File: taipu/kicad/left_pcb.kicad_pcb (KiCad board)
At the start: 2 copper layers, 145 x 92.4 mm, 52 parts

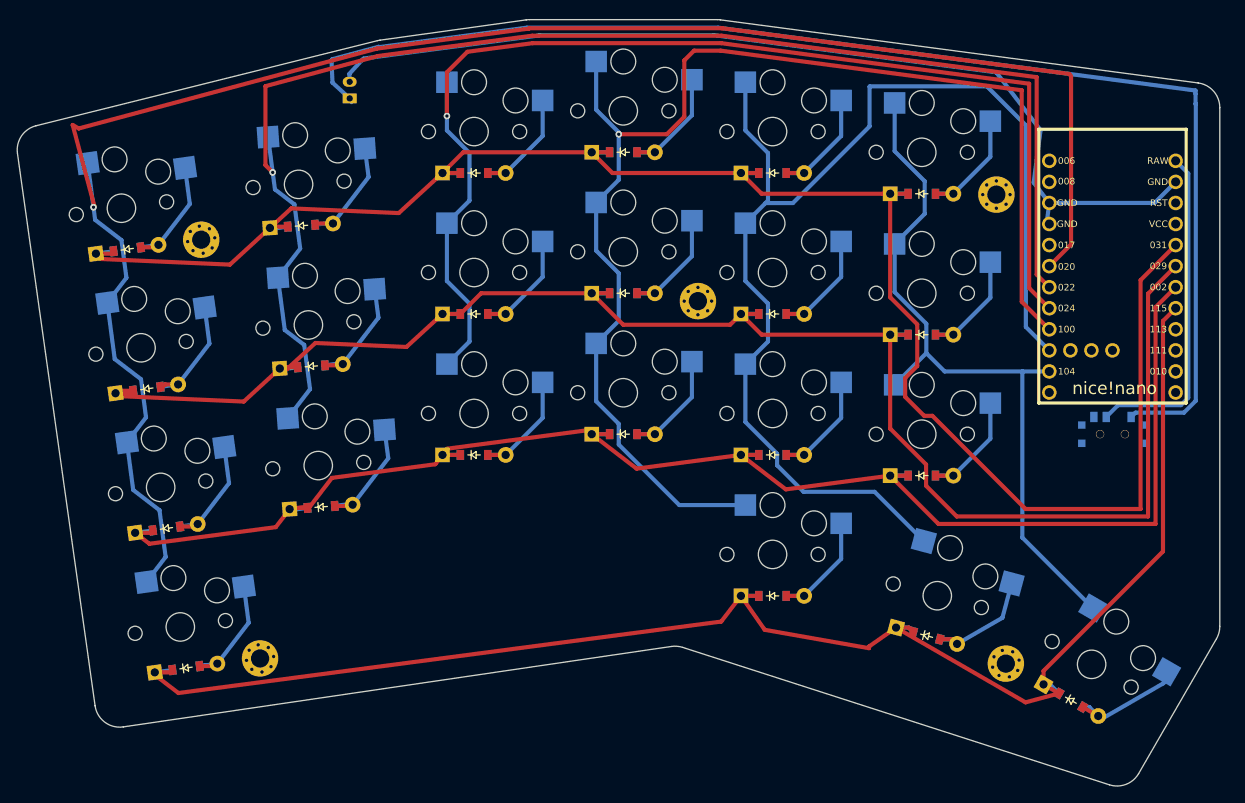
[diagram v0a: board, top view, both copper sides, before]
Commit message: better batery placement
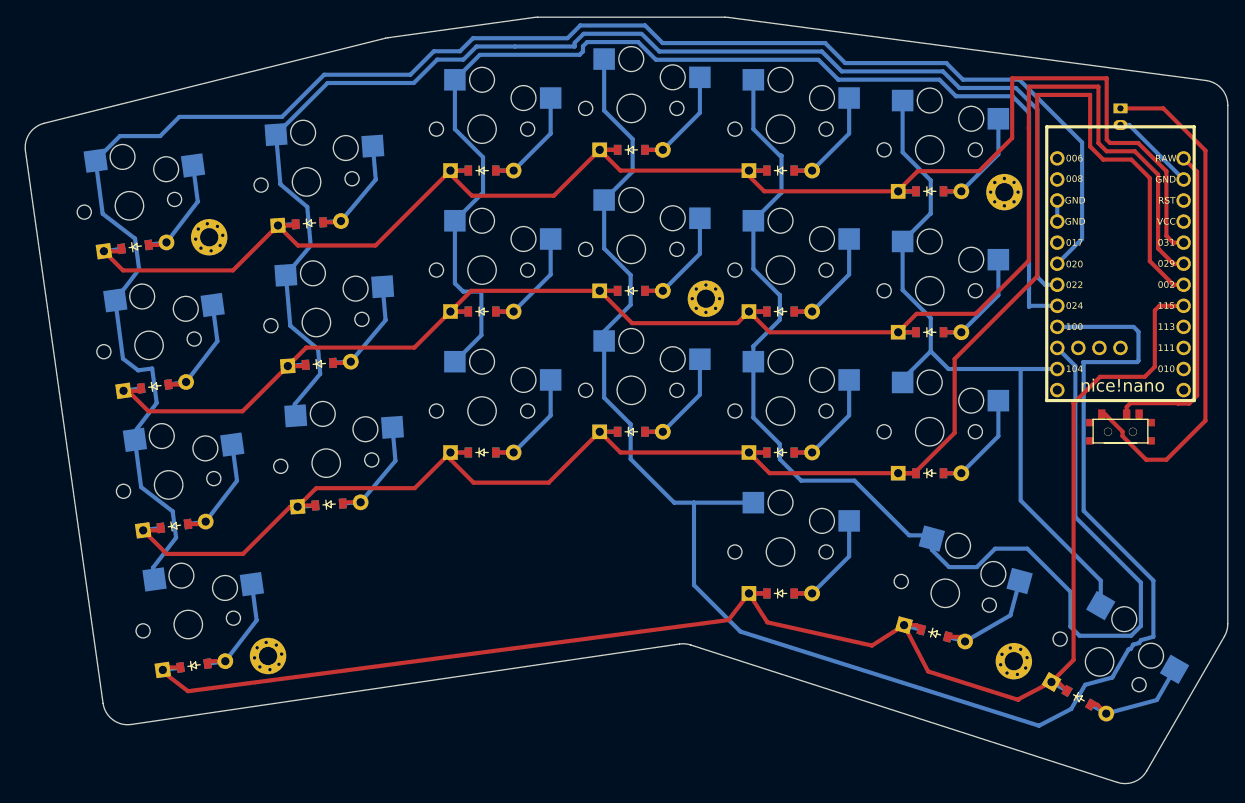
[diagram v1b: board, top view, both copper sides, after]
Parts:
- moved JST1 93.0 mm to (199.5, 87.0), turned to -90 degrees
- moved S5 1.01 mm to (103.7, 128.8)
- moved S6 1.01 mm to (102.5, 111.9)
- moved D16 1.01 mm to (158.5, 110.5)
- moved _1 1.01 mm to (89.6, 101.6)
- moved S19 1.01 mm to (176.5, 108.0)
- moved S17 1.01 mm to (158.5, 88.5)
- moved D9 1.01 mm to (122.5, 110.5)
- moved D2 1.01 mm to (85.4, 136.4)
- moved D14 1.01 mm to (158.5, 144.5)
- moved S3 1.01 mm to (82.3, 114.6)
- moved D19 1.01 mm to (176.5, 113.0)
- moved S20 1.01 mm to (176.5, 91.0)
- moved D13 1.01 mm to (140.5, 91.0)
- moved T1 1.01 mm to (199.5, 125.0)
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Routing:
- net GND: track 117.4 -> 12.9 mm
- net pos: track 157.2 -> 62.1 mm
- net P100: track 157.4 -> 203.2 mm, vias 1 -> 0
- net P002: track 189.1 -> 220.4 mm
- net P031: track 224.8 -> 197.6 mm
- net P020: track 215.7 -> 207.7 mm, vias 1 -> 0
- net P022: track 169.0 -> 163.1 mm, vias 1 -> 0
- net P011: track 144.1 -> 148.4 mm
- net P115: track 188.0 -> 192.3 mm
- net P029: track 210.4 -> 206.9 mm
- net outer_mod: track 16.6 -> 15.0 mm
- net P024: track 143.5 -> 142.6 mm, vias 1 -> 0
- net RAW: track 40.1 -> 39.3 mm

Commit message: add logo
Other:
- board text added: "タイプ"
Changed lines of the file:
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@@
 			(outputformat 1)
 			(mirror no)
-			(drillshape 1)
+			(drillshape 0)
 			(scaleselection 1)
-			(outputdirectory "")
+			(outputdirectory "left_gerbers/")
 		)
 	)
@@
 		(layer "Edge.Cuts")
 	)
+	(gr_text "タイプ"
+		(at 105 156.2 10)
+		(layer "F.SilkS")
+		(effects
+			(font
+				(size 13 13)
+				(thickness 1.625)
+			)
+			(justify left bottom)
+		)
+	)
 	(segment
